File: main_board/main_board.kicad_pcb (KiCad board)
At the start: 2 copper layers, 160 x 110 mm, 90 parts, among them IC1 MP2722GRH-0000-Z, IC2 MP3429GL-Z, IC3 NX3DV42GU, J1 USB3_A, J22 690-019-298-412, J3 Bus_M.2_Socket_M, J4 USB_B_Micro, J5 USB_C_Receptacle_USB2.0, SW1 Right angle Tact button, U1 AP3441SHE-7B, U12 RT9742SNGV, U2 ASEK-32.768KHZ-L-R-T, U3 ATmega32U4-M, U5 74LVC1G07SE-7, U6 AP22653W6, Y1 Crystal

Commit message: Finalize power management
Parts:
- removed D1: LED Red, LED_SMD:LED_0805_2012Metric_Pad1.15x1.40mm_HandSolder
- removed D2: LED Green, LED_SMD:LED_0805_2012Metric_Pad1.15x1.40mm_HandSolder
- removed R1, R10: 1k, Resistor_SMD:R_0805_2012Metric_Pad1.20x1.40mm_HandSolder
- removed U5: 74LVC1G07SE-7, Package_TO_SOT_SMD:SOT-353_SC-70-5
- added C41: 100n, Capacitor_SMD:C_0805_2012Metric_Pad1.18x1.45mm_HandSolder, F.Cu at (73.9, 32.5)
- added IC4: AP2204R-3.3TRG1, 000_custom:AP2204R33TRG1, F.Cu at (73.0, 29.8)
- moved C11 7.57 mm to (126.6, 121.8), turned to 90 degrees
- moved C10 7.51 mm to (128.8, 121.8), turned to 90 degrees
- moved C32 5.29 mm to (90.8, 27.6)
- moved C31 5.20 mm to (93.1, 34.6)
- moved C36 5.20 mm to (133.7, 35.1)
- moved C24 5.20 mm to (123.2, 28.6)
- moved C25 5.20 mm to (125.2, 39.1)
- moved C33 5.20 mm to (117.5, 38.9)
- moved C34 5.20 mm to (117.5, 40.9)
- moved C35 5.20 mm to (117.5, 42.8)
- moved IC2 5.20 mm to (126.0, 34.5)
- moved L3 5.20 mm to (116.9, 32.4)
- moved R7 5.20 mm to (127.8, 39.2)
- moved C26 5.20 mm to (123.3, 39.1)
- moved C27 5.20 mm to (126.8, 42.8)
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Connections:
- C32 pad 2: /Battery management/V_SYS -> /Battery management/PMIC_3.3V
- IC1 pad 15: /Battery management/IIC_SCL -> /Battery management/IIC_SDA
- IC1 pad 16: /Battery management/IIC_SDA -> /Battery management/IIC_SCL
- IC3 pad 4: /Battery management/USBC_MX1_USB2_P -> /Battery management/USBC_MX2_USB2_N
- IC3 pad 5: /Battery management/USBC_MX1_USB2_N -> /Battery management/USBC_MX2_USB2_P
- IC3 pad 6: /Battery management/USBC_MX2_USB2_P -> /Battery management/USBC_MX1_USB2_P
- IC3 pad 7: /Battery management/USBC_MX2_USB2_N -> /Battery management/USBC_MX1_USB2_N
- IC3 pad 9: /Battery management/V_SYS -> /Battery management/PMIC_3.3V
- J1 pad MH1: (no net) -> GND
- J1 pad MH2: (no net) -> GND
- J4 pad 1: /Battery management/V_SYS -> /Battery management/PMIC_3.3V
- J5 pad G1: (no net) -> GND
- J5 pad G2: (no net) -> GND
- J5 pad G3: (no net) -> GND
- J5 pad G4: (no net) -> GND
- Module1 pad 99: /CM5_GPIO/CM5_PMIC_EN -> /Battery management/CM5_PMIC_EN
- R17 pad 1: Net-(IC2-EN) -> GND
- U3 pad 12: /Battery management/V_SYS -> /Battery management/PMIC_3.3V
- U3 pad 13: /Battery management/V_SYS -> /Battery management/PMIC_3.3V
- U3 pad 14: /Battery management/V_SYS -> /Battery management/PMIC_3.3V
- U3 pad 18: /Battery management/IIC_SDA -> /Battery management/IIC_SCL
- U3 pad 19: /Battery management/IIC_SCL -> /Battery management/IIC_SDA
- U3 pad 2: /Battery management/V_SYS -> /Battery management/PMIC_3.3V
- U3 pad 24: /Battery management/V_SYS -> /Battery management/PMIC_3.3V
- U3 pad 30: unconnected-(U3-PB6-Pad30) -> /Battery management/CM5_PMIC_EN
- U3 pad 34: /Battery management/V_SYS -> /Battery management/PMIC_3.3V
- U3 pad 44: /Battery management/V_SYS -> /Battery management/PMIC_3.3V
- U3 pad 7: /Battery management/V_SYS -> /Battery management/PMIC_3.3V
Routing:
- net /Battery management/PMIC_3.3V: track 0.00 -> 91.7 mm, vias 0 -> 4
- net /Battery management/V_SYS: track 87.6 -> 7.39 mm, vias 3 -> 0
- net /Battery management/IIC_SCL: track 37.0 -> 91.7 mm, vias 0 -> 2
- net /Battery management/IIC_SDA: track 38.4 -> 81.2 mm, vias 0 -> 2
- net /Battery management/+5V: track 527.4 -> 563.5 mm
- net /Battery management/CM5_PMIC_EN: track 0.00 -> 30.2 mm
- net /Battery management/USBC_MX2_USB2_P: track 30.8 -> 54.4 mm, vias 2 -> 0
- net /Battery management/USBC_MX2_USB2_N: track 30.5 -> 53.6 mm, vias 2 -> 0
- net /CM5_GPIO/+3.3v: track 20.4 -> 2.67 mm
- net /CM5_GPIO/LED_nACT: track 11.7 -> 0.00 mm
- net /Battery management/VBAT: track 142.8 -> 153.9 mm
- net /Battery management/VIN: track 33.7 -> 39.7 mm
- net /CM5_HighSpeed/PCIE_PWR_EN: track 118.1 -> 123.9 mm
- net /Battery management/PMIC INTERRUPT: track 24.4 -> 29.9 mm
- net /Battery management/CC1: track 25.6 -> 21.0 mm
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- added copper zone on B.Cu, net /Battery management/PMIC_3.3V
- removed copper zone on B.Cu, net /Battery management/V_SYS
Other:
- rule pad_to_mask_clearance: 0 -> 0.05

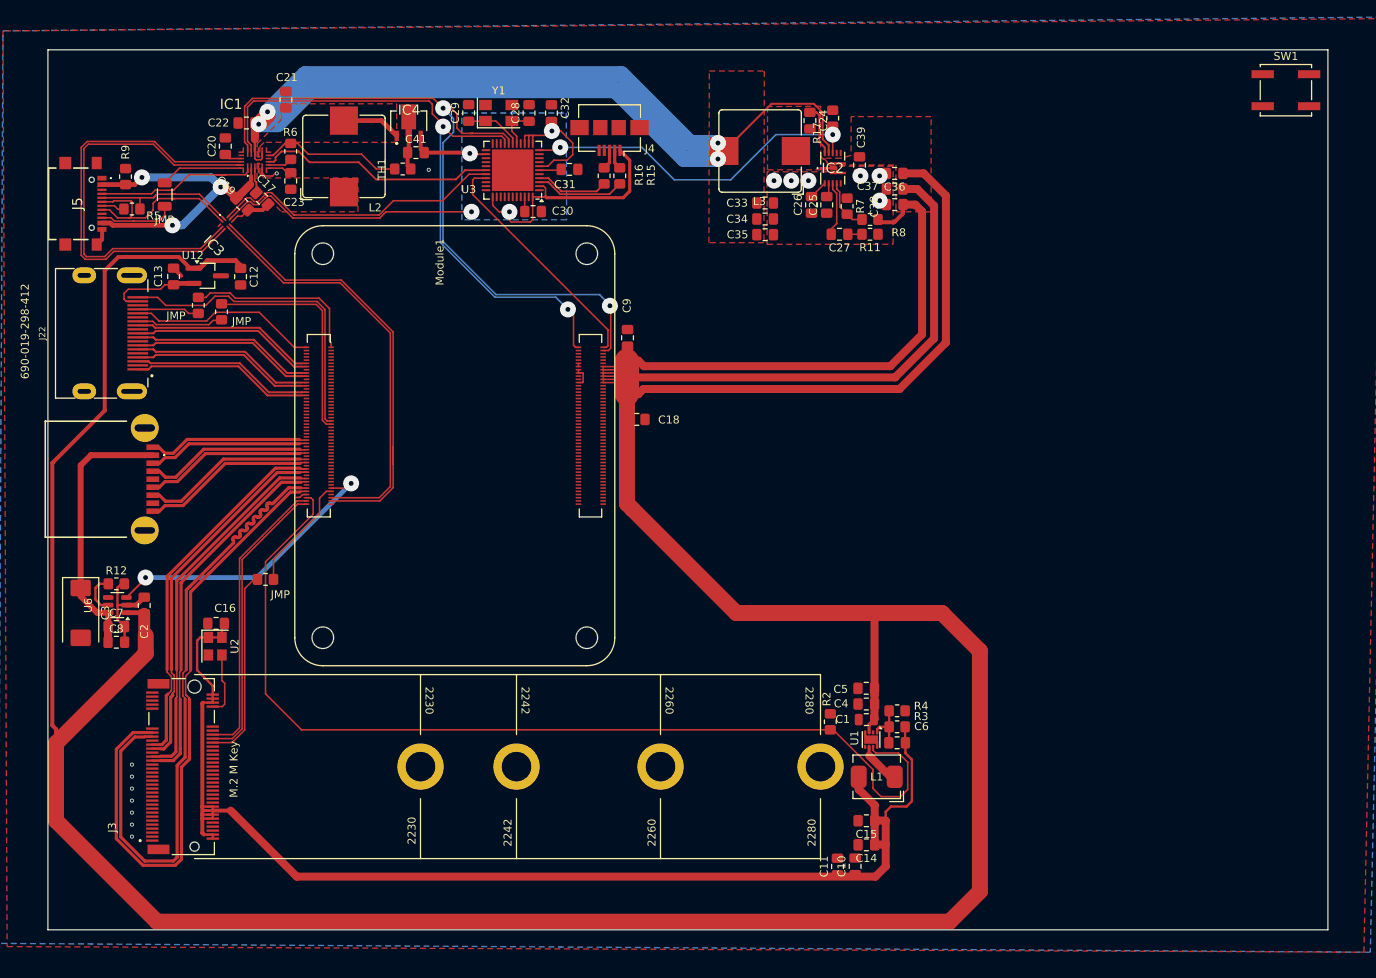
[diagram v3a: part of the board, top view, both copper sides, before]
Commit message: Start reouting USB hub
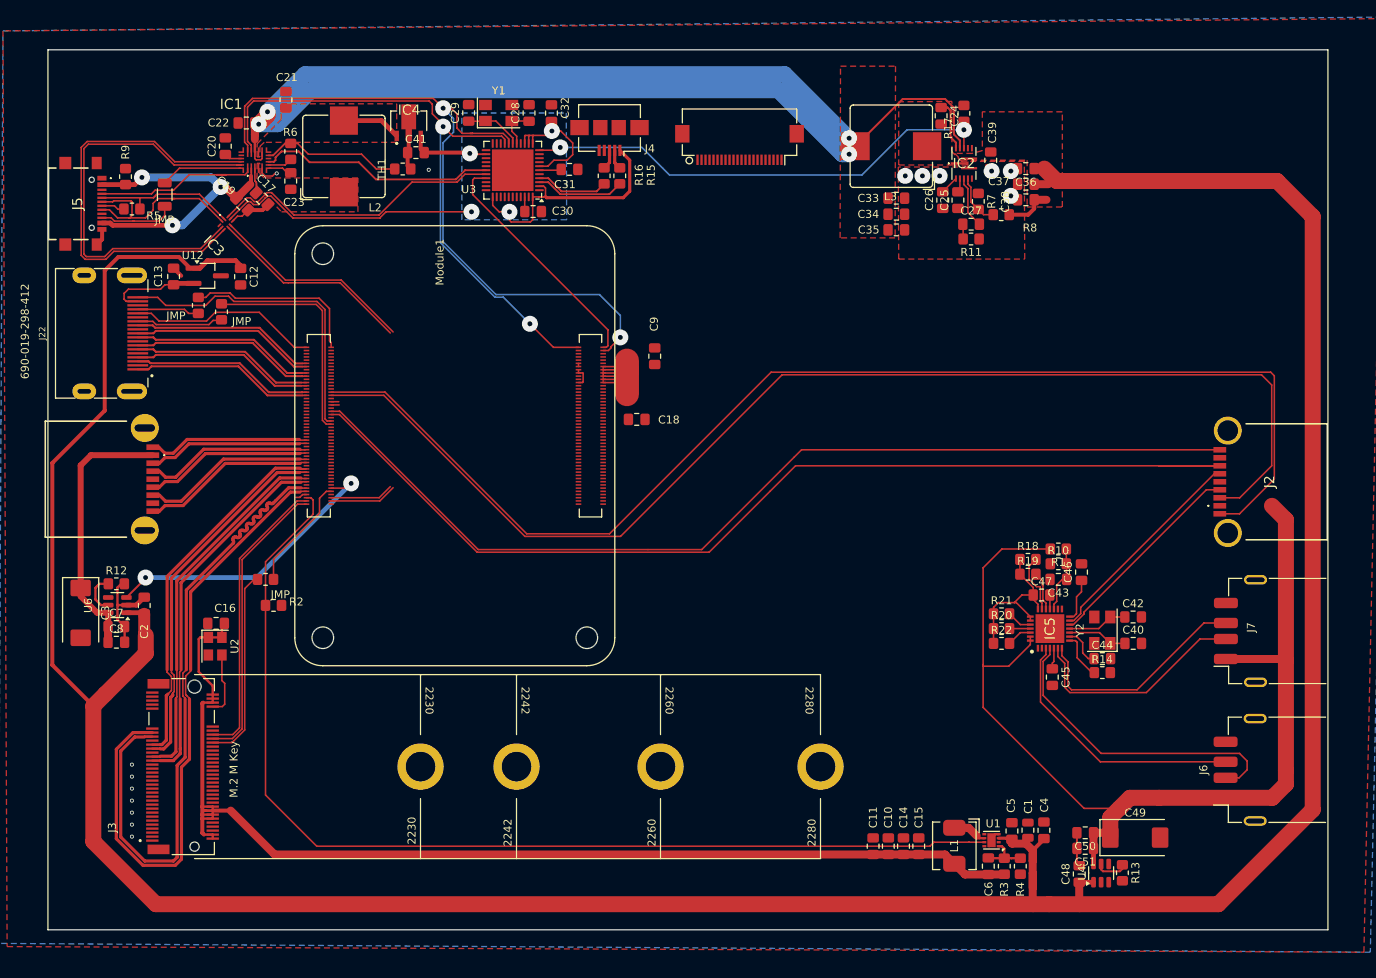
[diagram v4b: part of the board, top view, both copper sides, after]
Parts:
- removed SW1: Right angle Tact button, Button_Switch_SMD:SW_Push_1P1T_NO_CK_KSC7xxJ
- added C40: 22p, Capacitor_SMD:C_0805_2012Metric_Pad1.18x1.45mm_HandSolder, F.Cu at (163.6, 93.9)
- added C42: 22p, Capacitor_SMD:C_0805_2012Metric_Pad1.18x1.45mm_HandSolder, F.Cu at (163.6, 90.6)
- added C43: 1u, Capacitor_SMD:C_0805_2012Metric_Pad1.18x1.45mm_HandSolder, F.Cu at (154.2, 85.9)
- added C44: 100n, Capacitor_SMD:C_0805_2012Metric_Pad1.18x1.45mm_HandSolder, F.Cu at (159.7, 95.8)
- added C45: 100n, Capacitor_SMD:C_0805_2012Metric_Pad1.18x1.45mm_HandSolder, F.Cu at (153.4, 98.1)
- added C46: 100n, Capacitor_SMD:C_0805_2012Metric_Pad1.18x1.45mm_HandSolder, F.Cu at (157.1, 85.0)
- added C47: 100n, Capacitor_SMD:C_0805_2012Metric_Pad1.18x1.45mm_HandSolder, F.Cu at (152.1, 87.8)
- added C48: 10u, Capacitor_SMD:C_0805_2012Metric_Pad1.18x1.45mm_HandSolder, F.Cu at (156.8, 122.7)
- added C49: 100uF, Capacitor_Tantalum_SMD:CP_EIA-7343-31_Kemet-D, F.Cu at (163.8, 118.2)
- added C50: 10u, Capacitor_SMD:C_0805_2012Metric_Pad1.18x1.45mm_HandSolder, F.Cu at (157.6, 117.6)
- added C51: 10u, Capacitor_SMD:C_0805_2012Metric_Pad1.18x1.45mm_HandSolder, F.Cu at (157.6, 119.5)
- added IC5: CY7C65632-28LTXC, 000_custom:QFN50P500X500X80-29N-D, F.Cu at (153.2, 92.0)
- added J2: USB3_A, 000_custom:U3BU1ASMT1, F.Cu at (180.6, 73.7)
- added J6: USB_A, Connector_USB:USB_A_Receptacle_GCT_USB1046, F.Cu at (182.4, 109.7)
- added J7: USB_A, Connector_USB:USB_A_Receptacle_GCT_USB1046, F.Cu at (182.4, 92.3)
- added J8: Conn_01x22_Female, CM5IO:Hirose_FH12-22S-0.5SH_1x22-1MP_P0.50mm_Horizontal, F.Cu at (114.3, 31.6)
- added R1: 1k, Resistor_SMD:R_0805_2012Metric_Pad1.20x1.40mm_HandSolder, F.Cu at (154.2, 82.1)
- added R10: 47k, Resistor_SMD:R_0805_2012Metric_Pad1.20x1.40mm_HandSolder, F.Cu at (154.2, 84.0)
- added R13: 15K 1%, Resistor_SMD:R_0805_2012Metric_Pad1.20x1.40mm_HandSolder, F.Cu at (162.2, 122.6)
- added R14: 650R, Resistor_SMD:R_0805_2012Metric_Pad1.20x1.40mm_HandSolder, F.Cu at (159.7, 97.5)
- added R18: 10k, Resistor_SMD:R_0805_2012Metric_Pad1.20x1.40mm_HandSolder, F.Cu at (150.4, 83.4)
- added R19: 10k, Resistor_SMD:R_0805_2012Metric_Pad1.20x1.40mm_HandSolder, F.Cu at (150.4, 85.2)
- added R20: 10k, Resistor_SMD:R_0805_2012Metric_Pad1.20x1.40mm_HandSolder, F.Cu at (147.1, 92.0)
- added R21: 10k, Resistor_SMD:R_0805_2012Metric_Pad1.20x1.40mm_HandSolder, F.Cu at (147.1, 90.2)
- added R22: 100k, Resistor_SMD:R_0805_2012Metric_Pad1.20x1.40mm_HandSolder, F.Cu at (147.1, 93.9)
- added U4: AP22653W6, Package_TO_SOT_SMD:SOT-23-6, F.Cu at (159.5, 122.6)
- added Y2: Crystal, Crystal:Crystal_SMD_5032-4Pin_5.0x3.2mm, F.Cu at (159.7, 92.2)
- moved R2 71.1 mm to (56.1, 89.2), turned to 0 degrees
- moved C4 27.2 mm to (152.4, 117.3), turned to 90 degrees
- moved C5 25.5 mm to (148.4, 117.3), turned to 90 degrees
- moved R4 24.8 mm to (149.4, 121.8), turned to -90 degrees
- moved C1 24.5 mm to (150.4, 117.2), turned to 90 degrees
- moved R3 22.0 mm to (147.4, 121.8), turned to 90 degrees
- moved U1 19.6 mm to (145.8, 118.5), turned to 180 degrees
- moved C6 19.2 mm to (145.5, 121.8), turned to 90 degrees
- moved C27 16.5 mm to (143.3, 41.5), turned to 0 degrees
- moved C24 16.4 mm to (139.6, 27.9)
- moved C25 16.4 mm to (141.7, 38.5)
- moved C26 16.4 mm to (139.8, 38.5)
- moved C37 16.4 mm to (150.2, 36.5)
- moved C38 16.4 mm to (150.2, 38.5)
- moved C39 16.4 mm to (145.8, 33.5)
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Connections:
- J1 pad MH1: GND -> (no net)
- J1 pad MH2: GND -> (no net)
- J5 pad G1: GND -> (no net)
- J5 pad G2: GND -> (no net)
- J5 pad G3: GND -> (no net)
- J5 pad G4: GND -> (no net)
- Module1 pad 157: /CM5_HighSpeed/USB3-1-RX_N -> /CM5_HighSpeed/USB3_1_RX_N
- Module1 pad 159: /CM5_HighSpeed/USB3-1-RX_P -> /CM5_HighSpeed/USB3_1_RX_P
- Module1 pad 163: /CM5_HighSpeed/USB3-1-D_P -> /CM5_HighSpeed/USB3_1_DP
- Module1 pad 165: /CM5_HighSpeed/USB3-1-D_N -> /CM5_HighSpeed/USB3_1_DN
- Module1 pad 169: /CM5_HighSpeed/USB3-1-TX_N -> /CM5_HighSpeed/USB3_1_TX_N
- Module1 pad 171: /CM5_HighSpeed/USB3-1-TX_P -> /CM5_HighSpeed/USB3_1_TX_P
- Module1 pad 21: /CM5_GPIO/LED_nACT -> unconnected-(Module1A-LED_nACT-Pad21)
- Module1 pad 95: /CM5_GPIO/nPWR_LED -> unconnected-(Module1A-LED_nPWR-Pad95)
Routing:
- net /CM5_HighSpeed/USB3_1_TX_P: track 0.00 -> 155.3 mm
- net /CM5_HighSpeed/USB3_1_TX_N: track 0.00 -> 152.0 mm
- net /USB hub/VBUS: track 0.00 -> 147.0 mm
- net /CM5_HighSpeed/USB3_1_RX_N: track 0.00 -> 130.3 mm
- net /Battery management/+5V: track 563.5 -> 440.0 mm
- net /CM5_HighSpeed/USB3_1_RX_P: track 0.00 -> 123.4 mm
- net Net-(IC5-DD+[1]): track 0.00 -> 39.4 mm
- net Net-(IC5-DD-[1]): track 0.00 -> 33.2 mm
- net /Battery management/VBAT: track 153.9 -> 186.2 mm
- net Net-(IC5-DD+[2]): track 0.00 -> 28.5 mm
- net Net-(IC5-DD-[2]): track 0.00 -> 28.4 mm
- net Net-(IC5-DD+[3]): track 0.00 -> 26.8 mm
- net Net-(IC5-DD-[3]): track 0.00 -> 25.9 mm
- net /PCIe-M2/M2_3v3: track 166.9 -> 142.2 mm
- net /Battery management/USBC_MX1_USB2_N: track 55.9 -> 34.3 mm
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
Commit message: Bunch more routing, mainly added MIPI interface, reworked power management a bit
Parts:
- removed C41: 100n, Capacitor_SMD:C_0805_2012Metric_Pad1.18x1.45mm_HandSolder
- removed IC4: AP2204R-3.3TRG1, 000_custom:AP2204R33TRG1
- removed J8: Conn_01x22_Female, CM5IO:Hirose_FH12-22S-0.5SH_1x22-1MP_P0.50mm_Horizontal
- added J10: Conn_01x22_Female, CM5IO:Hirose_FH12-22S-0.5SH_1x22-1MP_P0.50mm_Horizontal, F.Cu at (115.3, 30.9)
- added JMP: R_0805_2012Metric_Pad1.20x1.40mm_HandSolder, Resistor_SMD:R_0805_2012Metric_Pad1.20x1.40mm_HandSolder, F.Cu at (72.1, 33.8)
- added JMP: R_0805_2012Metric_Pad1.20x1.40mm_HandSolder, Resistor_SMD:R_0805_2012Metric_Pad1.20x1.40mm_HandSolder, F.Cu at (113.6, 41.8)
- added R23: 2.2K 1%, Resistor_SMD:R_0805_2012Metric_Pad1.20x1.40mm_HandSolder, F.Cu at (118.0, 36.5)
- added R24: 2K2, Resistor_SMD:R_0805_2012Metric_Pad1.20x1.40mm_HandSolder, F.Cu at (116.2, 36.5)
- added R25: 2K2, Resistor_SMD:R_0805_2012Metric_Pad1.20x1.40mm_HandSolder, F.Cu at (117.1, 39.2)
- moved TH1 8.98 mm to (69.9, 25.9), turned to 90 degrees
- moved C18 3.07 mm to (104.0, 64.0), turned to -90 degrees
- moved R17 2.97 mm to (139.5, 27.0), turned to -90 degrees
- moved C19 2.83 mm to (49.4, 39.0)
- moved C20 2.83 mm to (47.2, 31.8)
- moved C24 2.83 mm to (136.7, 27.9)
- moved C25 2.83 mm to (138.8, 38.5)
- moved C26 2.83 mm to (136.9, 38.5)
- moved C27 2.83 mm to (140.5, 41.5)
- moved C30 2.83 mm to (85.7, 39.9)
- moved C32 2.83 mm to (88.0, 27.6)
- moved C37 2.83 mm to (147.3, 36.5)
- moved C38 2.83 mm to (147.3, 38.5)
- moved C39 2.83 mm to (142.9, 33.5)
- moved IC1 2.83 mm to (50.9, 33.5)
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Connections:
- C32 pad 2: /Battery management/PMIC_3.3V -> /Battery management/VBAT
- IC3 pad 9: /Battery management/PMIC_3.3V -> /Battery management/USB_MUX_VCC
- J4 pad 1: /Battery management/PMIC_3.3V -> Net-(J4-VBUS)
- Module1 pad 115: unconnected-(Module1B-MIPI0_D0_N-Pad115) -> /CM5_HighSpeed/DPHY0_D0_N
- Module1 pad 117: unconnected-(Module1B-MIPI0_D0_P-Pad117) -> /CM5_HighSpeed/DPHY0_D0_P
- Module1 pad 121: unconnected-(Module1B-MIPI0_D1_N-Pad121) -> /CM5_HighSpeed/DPHY0_D1_N
- Module1 pad 123: unconnected-(Module1B-MIPI0_D1_P-Pad123) -> /CM5_HighSpeed/DPHY0_D1_P
- Module1 pad 127: unconnected-(Module1B-MIPI0_C_N-Pad127) -> /CM5_HighSpeed/DPHY0_C_N
- Module1 pad 129: unconnected-(Module1B-MIPI0_C_P-Pad129) -> /CM5_HighSpeed/DPHY0_C_P
- Module1 pad 133: unconnected-(Module1B-MIPI0_D2_N-Pad133) -> /CM5_HighSpeed/DPHY0_D2_N
- Module1 pad 135: unconnected-(Module1B-MIPI0_D2_P-Pad135) -> /CM5_HighSpeed/DPHY0_D2_P
- Module1 pad 139: unconnected-(Module1B-MIPI0_D3_N-Pad139) -> /CM5_HighSpeed/DPHY0_D3_N
- Module1 pad 141: unconnected-(Module1B-MIPI0_D3_P-Pad141) -> /CM5_HighSpeed/DPHY0_D3_P
- Module1 pad 143: unconnected-(Module1B-HDMI1_HOTPLUG-Pad143) -> /CM5_HighSpeed/HDMI1_HOTPLUG
- Module1 pad 145: unconnected-(Module1B-HDMI1_SDA-Pad145) -> /CM5_HighSpeed/HDMI1_SDA
- Module1 pad 146: unconnected-(Module1B-HDMI1_TX2_P-Pad146) -> /CM5_HighSpeed/HDMI1_D2_P
- Module1 pad 147: unconnected-(Module1B-HDMI1_SCL-Pad147) -> /CM5_HighSpeed/HDMI1_SCL
- Module1 pad 148: unconnected-(Module1B-HDMI1_TX2_N-Pad148) -> /CM5_HighSpeed/HDMI1_D2_N
- Module1 pad 149: unconnected-(Module1B-HDMI1_CEC-Pad149) -> /CM5_HighSpeed/HDMI1_CEC
- Module1 pad 152: unconnected-(Module1B-HDMI1_TX1_P-Pad152) -> /CM5_HighSpeed/HDMI1_D1_P
- Module1 pad 154: unconnected-(Module1B-HDMI1_TX1_N-Pad154) -> /CM5_HighSpeed/HDMI1_D1_N
- Module1 pad 158: unconnected-(Module1B-HDMI1_TX0_P-Pad158) -> /CM5_HighSpeed/HDMI1_D0_P
- Module1 pad 160: unconnected-(Module1B-HDMI1_TX0_N-Pad160) -> /CM5_HighSpeed/HDMI1_D0_N
- Module1 pad 164: unconnected-(Module1B-HDMI1_CLK_P-Pad164) -> /CM5_HighSpeed/HDMI1_CK_P
- Module1 pad 166: unconnected-(Module1B-HDMI1_CLK_N-Pad166) -> /CM5_HighSpeed/HDMI1_CK_N
- Module1 pad 175: unconnected-(Module1B-MIPI1_D0_N-Pad175) -> /CM5_HighSpeed/DPHY1_D0_N
- Module1 pad 177: unconnected-(Module1B-MIPI1_D0_P-Pad177) -> /CM5_HighSpeed/DPHY1_D0_P
- Module1 pad 181: unconnected-(Module1B-MIPI1_D1_N-Pad181) -> /CM5_HighSpeed/DPHY1_D1_N
- Module1 pad 183: unconnected-(Module1B-MIPI1_D1_P-Pad183) -> /CM5_HighSpeed/DPHY1_D1_P
- Module1 pad 187: unconnected-(Module1B-MIPI1_C_N-Pad187) -> /CM5_HighSpeed/DPHY1_C_N
- Module1 pad 189: unconnected-(Module1B-MIPI1_C_P-Pad189) -> /CM5_HighSpeed/DPHY1_C_P
- Module1 pad 193: unconnected-(Module1B-MIPI1_D2_N-Pad193) -> /CM5_HighSpeed/DPHY1_D2_N
- Module1 pad 194: unconnected-(Module1B-MIPI1_D3_N-Pad194) -> /CM5_HighSpeed/DPHY1_D3_N
- Module1 pad 195: unconnected-(Module1B-MIPI1_D2_P-Pad195) -> /CM5_HighSpeed/DPHY1_D2_P
- Module1 pad 196: unconnected-(Module1B-MIPI1_D3_P-Pad196) -> /CM5_HighSpeed/DPHY1_D3_P
- Module1 pad 35: unconnected-(Module1A-ID_SC-Pad35) -> /CM5_GPIO/DPHY1_SCL
- Module1 pad 36: unconnected-(Module1A-ID_SD-Pad36) -> /CM5_GPIO/DPHY1_SDA
- R17 pad 2: /Battery management/VBAT -> Net-(IC2-EN)
- U3 pad 10: unconnected-(U3-PB2-Pad10) -> GND
- U3 pad 12: /Battery management/PMIC_3.3V -> /Battery management/VBAT
- U3 pad 13: /Battery management/PMIC_3.3V -> /Battery management/VBAT
- U3 pad 14: /Battery management/PMIC_3.3V -> /Battery management/VBAT
- U3 pad 2: /Battery management/PMIC_3.3V -> /Battery management/VBAT
- U3 pad 24: /Battery management/PMIC_3.3V -> /Battery management/VBAT
- U3 pad 25: unconnected-(U3-PD4-Pad25) -> GND
- U3 pad 26: unconnected-(U3-PD6-Pad26) -> GND
- U3 pad 27: unconnected-(U3-PD7-Pad27) -> GND
- U3 pad 31: unconnected-(U3-PC6-Pad31) -> /Battery management/USB_MUX_VCC
- U3 pad 34: /Battery management/PMIC_3.3V -> /Battery management/VBAT
- U3 pad 44: /Battery management/PMIC_3.3V -> /Battery management/VBAT
- U3 pad 7: /Battery management/PMIC_3.3V -> Net-(J4-VBUS)
- U3 pad 8: unconnected-(U3-PB0-Pad8) -> GND
- U3 pad 9: unconnected-(U3-PB1-Pad9) -> GND
- U4 pad 3: /USB hub/VBUS_EN -> /CM5_HighSpeed/VBUS_EN
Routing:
- net GND: track 40.1 -> 400.5 mm, vias 15 -> 14
- net /CM5_HighSpeed/USB3_1_DP: track 1.01 -> 131.2 mm, vias 0 -> 2
- net /CM5_HighSpeed/USB3_1_DN: track 0.96 -> 129.7 mm, vias 0 -> 2
- net /CM5_HighSpeed/VBUS_EN: track 36.3 -> 162.8 mm, vias 2 -> 3
- net /CM5_HighSpeed/DPHY0_D3_P: track 0.00 -> 93.3 mm
- net /CM5_HighSpeed/DPHY0_D3_N: track 0.00 -> 92.7 mm
- net /Battery management/PMIC_3.3V: track 91.7 -> 0.00 mm, vias 4 -> 0
- net /CM5_HighSpeed/DPHY0_D2_P: track 0.00 -> 91.6 mm
- net /CM5_HighSpeed/DPHY0_D2_N: track 0.00 -> 91.0 mm
- net /CM5_HighSpeed/DPHY0_C_P: track 0.00 -> 89.8 mm
- net /CM5_HighSpeed/DPHY0_C_N: track 0.00 -> 89.2 mm
- net /CM5_HighSpeed/DPHY0_D1_P: track 0.00 -> 88.1 mm
- net /CM5_HighSpeed/DPHY0_D1_N: track 0.00 -> 87.5 mm
- net /CM5_HighSpeed/DPHY0_D0_P: track 0.00 -> 86.3 mm
- net /CM5_HighSpeed/DPHY0_D0_N: track 0.00 -> 85.8 mm
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- added copper zone on B.Cu, net /Battery management/VBAT
- removed copper zone on B.Cu, net /Battery management/PMIC_3.3V
